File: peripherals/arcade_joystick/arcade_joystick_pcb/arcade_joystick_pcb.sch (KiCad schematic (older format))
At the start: 6 parts, among them J1 PJ320A, J2 Mr_Joystick

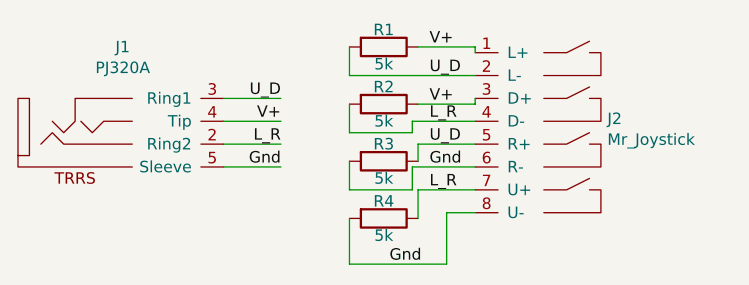
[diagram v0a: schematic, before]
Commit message: Updated arcade joystick pcb design
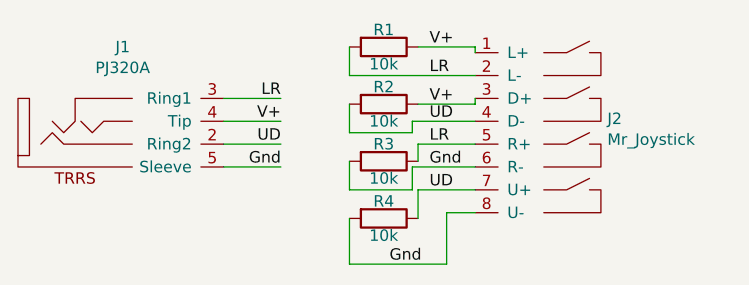
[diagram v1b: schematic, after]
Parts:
- R1, R2, R3, R4: value 5k -> 10k; footprint Resistor_SMD:R_1206_3216Metric_Pad1.42x1.75mm_HandSolder -> Resistor_SMD:R_1206_3216Metric; LCSC (none) -> C17902
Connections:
- net L_R renamed UD
- net U_D renamed LR
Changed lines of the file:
@@
 EESchema Schematic File Version 4
-LIBS:arcade_joystick_pcb-cache
 EELAYER 30 0
 EELAYER END
@@
 P 6350 2975
 F 0 "R1" V 6275 2975 50  0000 C CNN
-F 1 "5k" V 6425 2975 50  0000 C CNN
-F 2 "Resistor_SMD:R_1206_3216Metric_Pad1.42x1.75mm_HandSolder" V 6280 2975 50  0001 C CNN
+F 1 "10k" V 6425 2975 50  0000 C CNN
+F 2 "Resistor_SMD:R_1206_3216Metric" V 6280 2975 50  0001 C CNN
 F 3 "~" H 6350 2975 50  0001 C CNN
+F 4 "C17902" H 6350 2975 50  0001 C CNN "LCSC"
 	1    6350 2975
 	0    1    1    0
@@
 P 6350 3225
 F 0 "R2" V 6275 3225 50  0000 C CNN
-F 1 "5k" V 6425 3225 50  0000 C CNN
-F 2 "Resistor_SMD:R_1206_3216Metric_Pad1.42x1.75mm_HandSolder" V 6280 3225 50  0001 C CNN
+F 1 "10k" V 6425 3225 50  0000 C CNN
+F 2 "Resistor_SMD:R_1206_3216Metric" V 6280 3225 50  0001 C CNN
 F 3 "~" H 6350 3225 50  0001 C CNN
+F 4 "C17902" H 6350 3225 50  0001 C CNN "LCSC"
 	1    6350 3225
 	0    1    1    0
@@
 P 6350 3475
 F 0 "R3" V 6275 3475 50  0000 C CNN
-F 1 "5k" V 6425 3475 50  0000 C CNN
-F 2 "Resistor_SMD:R_1206_3216Metric_Pad1.42x1.75mm_HandSolder" V 6280 3475 50  0001 C CNN
+F 1 "10k" V 6425 3475 50  0000 C CNN
+F 2 "Resistor_SMD:R_1206_3216Metric" V 6280 3475 50  0001 C CNN
 F 3 "~" H 6350 3475 50  0001 C CNN
+F 4 "C17902" H 6350 3475 50  0001 C CNN "LCSC"
 	1    6350 3475
 	0    1    1    0
@@
 P 6350 3725
 F 0 "R4" V 6275 3725 50  0000 C CNN
-F 1 "5k" V 6425 3725 50  0000 C CNN
-F 2 "Resistor_SMD:R_1206_3216Metric_Pad1.42x1.75mm_HandSolder" V 6280 3725 50  0001 C CNN
+F 1 "10k" V 6425 3725 50  0000 C CNN
+F 2 "Resistor_SMD:R_1206_3216Metric" V 6280 3725 50  0001 C CNN
 F 3 "~" H 6350 3725 50  0001 C CNN
+F 4 "C17902" H 6350 3725 50  0001 C CNN "LCSC"
 	1    6350 3725
 	0    1    1    0
@@
 Gnd
 Text Label 6550 3100 0    50   ~ 0
-U_D
+LR
 Wire Wire Line
 	6500 3600 6500 3725
@@
 V+
 Text Label 6550 3300 0    50   ~ 0
-L_R
+UD
 Text Label 6550 3400 0    50   ~ 0
-U_D
+LR
 Text Label 6550 3600 0    50   ~ 0
-L_R
+UD
 Wire Wire Line
 	5650 3300 5900 3300
@@
 	5650 3200 5900 3200
 Text Label 5900 3200 2    50   ~ 0
-U_D
+LR
 Wire Wire Line
 	5650 3500 5900 3500
@@
 	5650 3400 5900 3400
 Text Label 5900 3400 2    50   ~ 0
-L_R
+UD
 $Comp
 L dbh_kicad_library:Mr_Joystick J2
